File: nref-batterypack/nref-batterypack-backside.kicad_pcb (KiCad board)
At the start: 2 copper layers, 75 x 17 mm, 8 parts, among them J1 C1+, J2 C2-, J3 C3+, J4 C4-, J5 FRONT_CONN

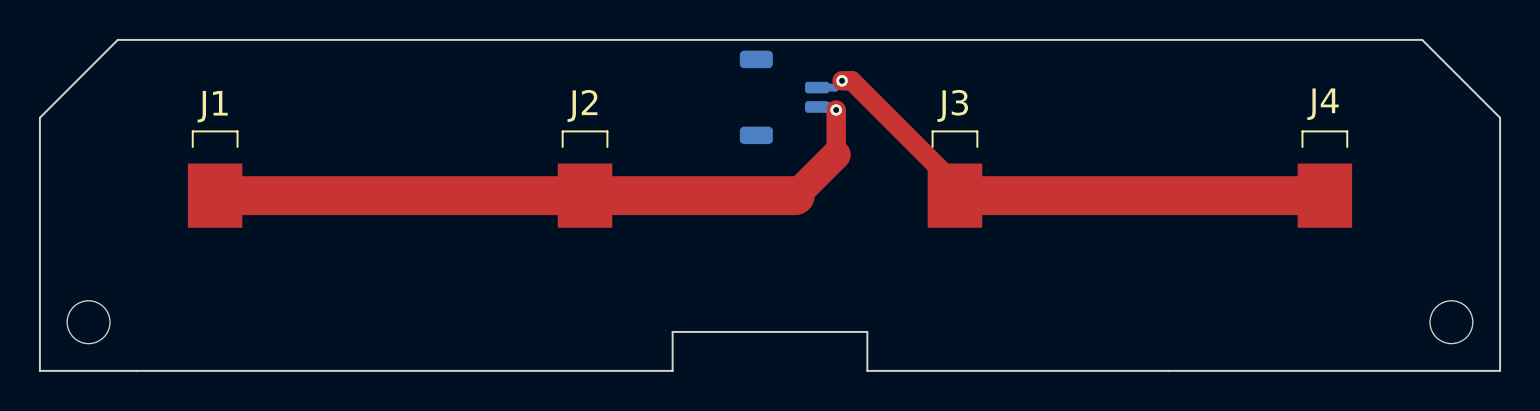
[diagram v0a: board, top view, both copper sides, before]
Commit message: batterypack front/back: update board outline/mounting holes
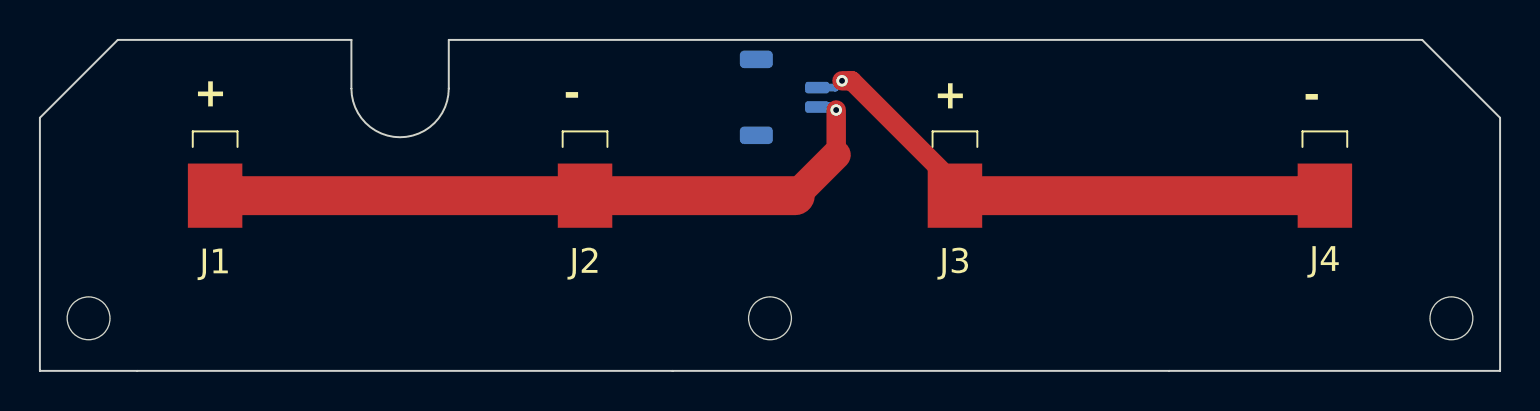
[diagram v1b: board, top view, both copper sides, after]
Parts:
- added H4: MountingHole, MountingHole:MountingHole_2.2mm_M2, F.Cu at (127.5, 97.3)
- moved H3 1.00 mm to (127.5, 92.3)
- moved H1 0.20 mm to (92.5, 97.3)
- moved H2 0.20 mm to (162.5, 97.3)
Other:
- outline, holes or cut-outs redrawn
- board text added: "+"
- board text added: "-"
